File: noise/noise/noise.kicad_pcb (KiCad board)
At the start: 2 copper layers, 38 parts, among them J1 Power Connector, J2 WHITE_OUT, J3 BLUE_OUT, J4 PINK_OUT, Q1 BC548, U1 TL074

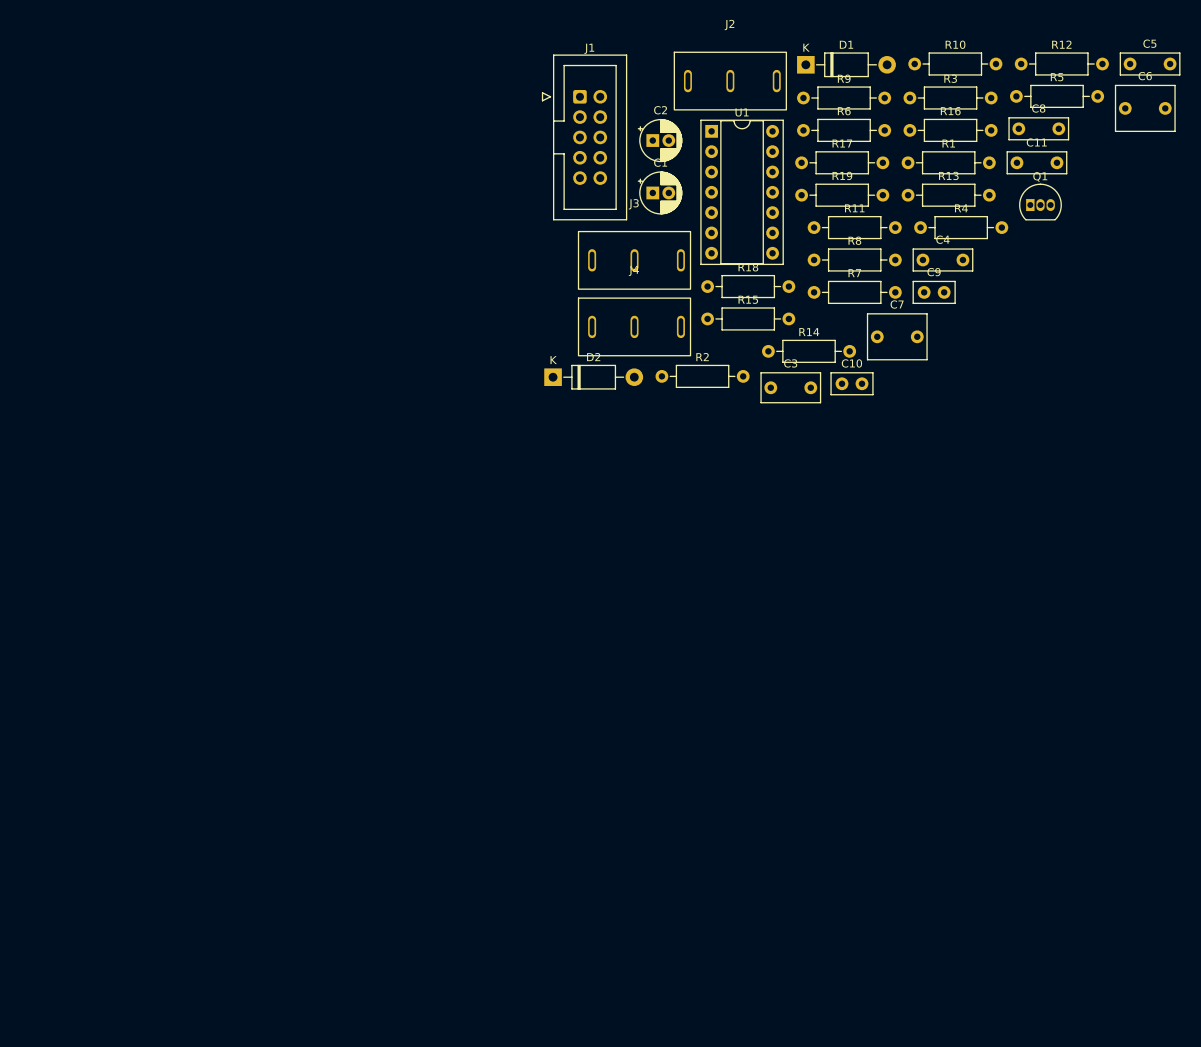
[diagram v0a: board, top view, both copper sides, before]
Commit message: Completed noise panel. Started on noise PCB
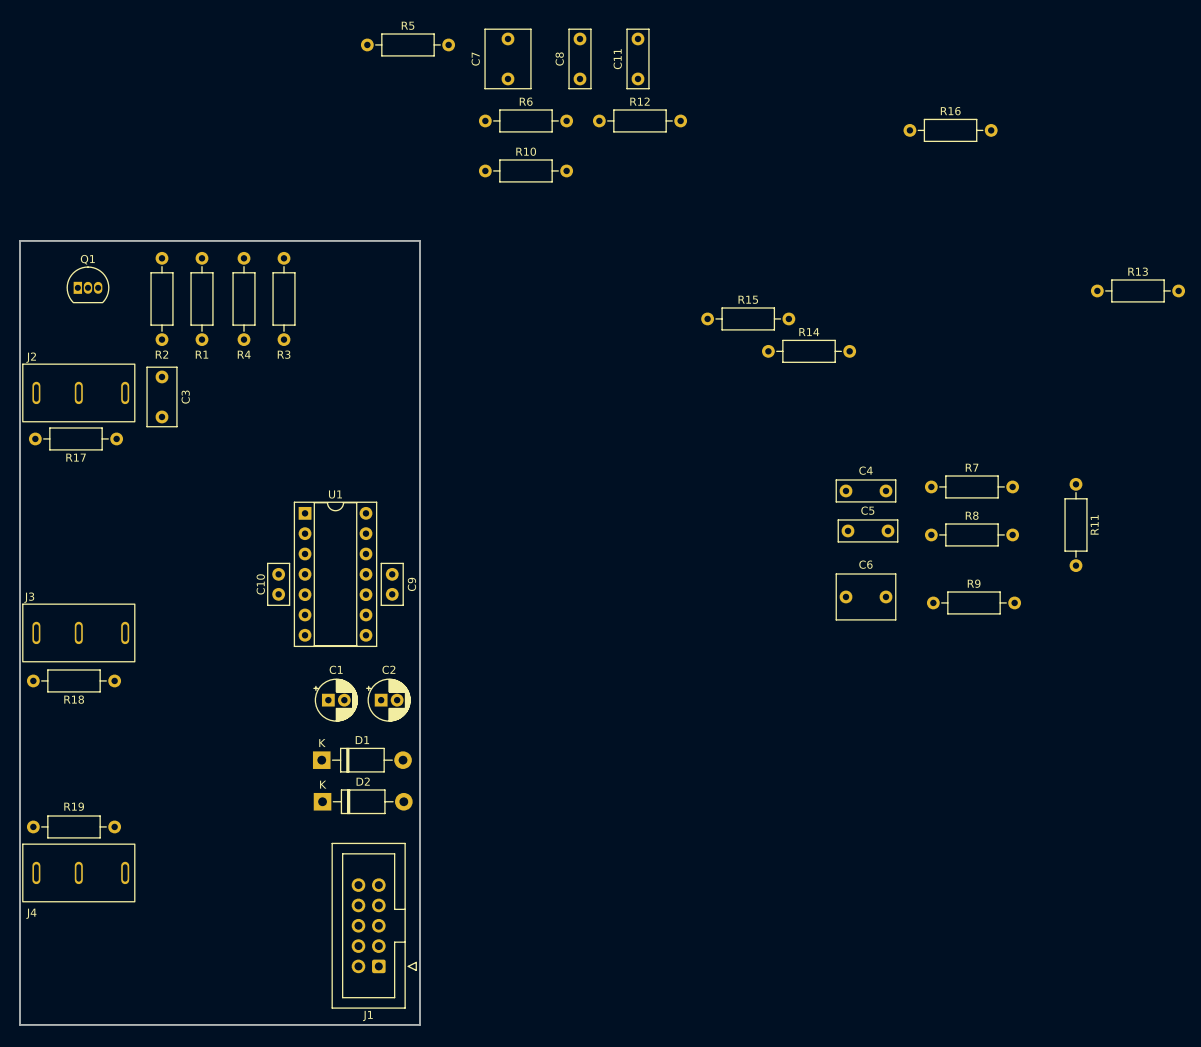
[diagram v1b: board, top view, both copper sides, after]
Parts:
- moved Q1 119.5 mm to (137.2, 50.9)
- moved R19 116.7 mm to (141.8, 118.2), turned to 180 degrees
- moved J1 111.6 mm to (174.9, 135.7), turned to 180 degrees
- moved D1 105.9 mm to (167.7, 109.9)
- moved J4 97.4 mm to (137.3, 124.0)
- moved R17 92.3 mm to (142.1, 69.8), turned to 180 degrees
- moved R1 91.0 mm to (152.8, 57.3), turned to 90 degrees
- moved J2 90.3 mm to (137.3, 64.0)
- moved R18 89.0 mm to (141.8, 100.0), turned to 180 degrees
- moved R4 85.7 mm to (158.0, 57.3), turned to 90 degrees
- moved R3 83.9 mm to (163.0, 57.3), turned to 90 degrees
- moved J3 83.6 mm to (137.3, 94.0)
- moved R5 81.4 mm to (173.4, 20.5)
- moved C2 77.8 mm to (175.1, 102.4)
- moved C3 76.1 mm to (147.8, 62.0), turned to -90 degrees
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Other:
- board outline added: 50 x 98 mm

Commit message: Completed noise pcb
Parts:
- moved R16 114.3 mm to (149.9, 100.0)
- moved C11 107.8 mm to (144.2, 112.2)
- moved C8 106.1 mm to (140.0, 112.2)
- moved C7 104.4 mm to (134.0, 112.2)
- moved R13 101.5 mm to (169.5, 86.7), turned to -90 degrees
- moved R11 96.4 mm to (166.0, 83.8), turned to 90 degrees
- moved R12 93.4 mm to (149.9, 107.2)
- moved R5 93.1 mm to (131.7, 103.8)
- moved R6 92.8 mm to (149.9, 114.5)
- moved R9 90.2 mm to (156.4, 69.2)
- moved R8 89.0 mm to (156.4, 65.5)
- moved R7 88.6 mm to (156.4, 61.8)
- moved R14 86.2 mm to (149.9, 103.6)
- moved R10 83.9 mm to (149.9, 110.9)
- moved C6 83.1 mm to (157.0, 56.5)
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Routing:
- net Net-(C4-Pad1): track 0.00 -> 85.1 mm
- net +12V: track 0.00 -> 84.5 mm
- net -12V: track 0.00 -> 72.0 mm
- net Net-(R16-Pad2): track 0.00 -> 56.9 mm
- net Net-(C11-Pad2): track 0.00 -> 38.6 mm
- net Net-(R11-Pad1): track 0.00 -> 34.6 mm
- net Net-(R15-Pad2): track 0.00 -> 32.5 mm
- net Net-(C3-Pad2): track 0.00 -> 31.7 mm
- net Net-(C3-Pad1): track 0.00 -> 28.0 mm
- net Net-(R3-Pad1): track 0.00 -> 25.3 mm
- net Net-(D2-Pad1): track 0.00 -> 24.0 mm
- net Net-(R14-Pad1): track 0.00 -> 19.5 mm
- net Net-(C7-Pad1): track 0.00 -> 16.9 mm
- net Net-(C4-Pad2): track 0.00 -> 16.6 mm
- net Net-(C5-Pad2): track 0.00 -> 16.6 mm
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- added copper zone on B.Cu, net GND
- added copper zone on F.Cu, net GND
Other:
- board size 50 x 98 mm -> 43 x 98 mm

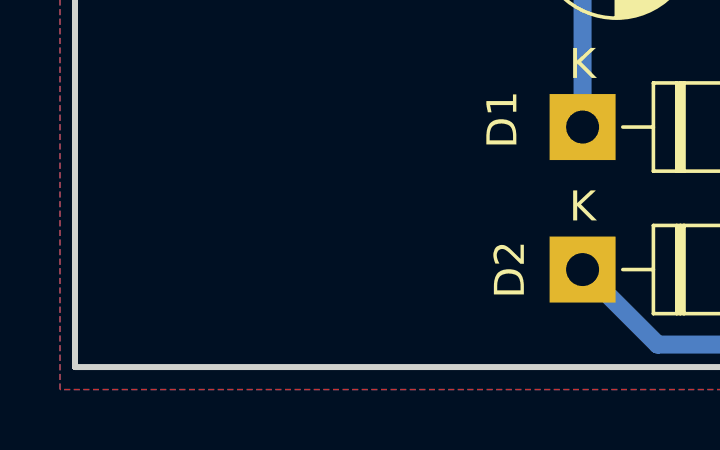
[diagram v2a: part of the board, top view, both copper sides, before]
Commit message: Added more text to noise pcb
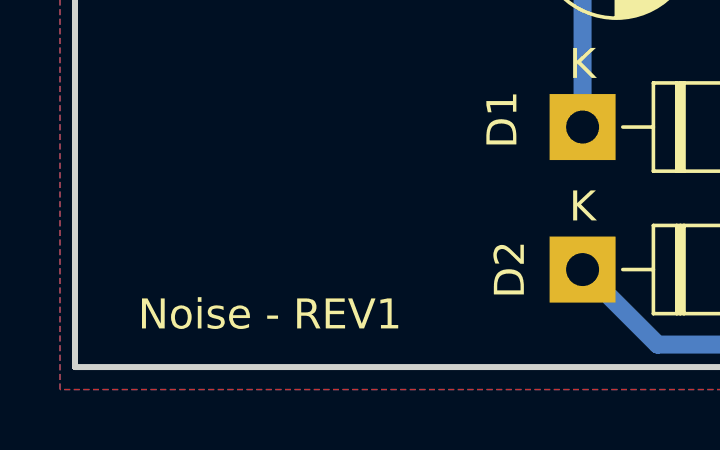
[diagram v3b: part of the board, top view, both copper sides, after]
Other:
- board text added: "Noise - REV1"
- board text added: "Northridge Devices - August 2022"
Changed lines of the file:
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@@
   )
   (gr_rect locked (start 130 45) (end 173 143) (layer "Edge.Cuts") (width 0.2) (fill none))
+  (gr_text "Northridge Devices  - August 2022" (at 170.5 59.75 90) (layer "B.SilkS")
+    (effects (font (size 1 1) (thickness 0.15)) (justify mirror))
+  )
+  (gr_text "Noise - REV1" (at 136.5 141.25) (layer "F.SilkS")
+    (effects (font (size 1 1) (thickness 0.15)))
+  )
   (dimension (type aligned) (layer "Cmts.User")
     (pts (xy 130 45) (xy 173 45))
